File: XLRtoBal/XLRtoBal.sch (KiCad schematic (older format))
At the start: 53 parts, among them J1 XLR3, J10 Conn_Coaxial, J11 Conn_Coaxial, J2 Conn_01x04, J3 Conn_01x04, J4 XLR3, J5 Conn_01x04, J6 Conn_01x01, J7 Conn_01x01, J8 Conn_01x01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

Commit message: Fixed XLR footprint
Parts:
- J1, J4: footprint XLRtoBal:XLR04WP -> XLRtoBal:IOXLR3FEH
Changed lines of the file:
@@
 F 0 "J1" H 2500 2100 50  0000 C CNN
 F 1 "XLR3" H 2550 1600 50  0000 C CNN
-F 2 "XLRtoBal:XLR04WP" H 2350 1850 50  0001 C CNN
+F 2 "XLRtoBal:IOXLR3FEH" H 2350 1850 50  0001 C CNN
 F 3 "" H 2350 1850 50  0001 C CNN
 	1    2350 1850
@@
 F 0 "J4" H 2500 4800 50  0000 C CNN
 F 1 "XLR3" H 2550 4300 50  0000 C CNN
-F 2 "XLRtoBal:XLR04WP" H 2350 4550 50  0001 C CNN
+F 2 "XLRtoBal:IOXLR3FEH" H 2350 4550 50  0001 C CNN
 F 3 "" H 2350 4550 50  0001 C CNN
 	1    2350 4550

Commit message: Changed bootstrap capacitor
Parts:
- removed C17, C5: CB, Capacitors_THT:C_Disc_D5.0mm_W2.5mm_P5.00mm, symbol C_Small
- added C17, C5: 220 uF, Capacitors_THT:CP_Radial_D8.0mm_P5.00mm, symbol CP_Small
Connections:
- net at JP1.2, U1.5 (CM): now also C5.2
- net at J2.2 (Pin_2), U1.8 (CMOUT): now also C5.1
- net at JP2.2, U2.5 (CM): now also C17.2
- net at J5.2 (Pin_2), U2.8 (CMOUT): now also C17.1
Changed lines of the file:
@@
-$EndComp
-$Comp
-L C_Small C5
-U 1 1 5F3D4D81
-P 5350 2850
-F 0 "C5" V 5450 2800 50  0000 L CNN
-F 1 "CB" V 5200 2800 50  0000 L CNN
-F 2 "Capacitors_THT:C_Disc_D5.0mm_W2.5mm_P5.00mm" H 5350 2850 50  0001 C CNN
-F 3 "" H 5350 2850 50  0001 C CNN
-	1    5350 2850
-	0    -1   -1   0
 $EndComp
 $Comp
@@
 	1    0    0    -1
 $EndComp
-$Comp
-L C_Small C17
-U 1 1 5F3DABDA
-P 5350 5550
-F 0 "C17" V 5450 5500 50  0000 L CNN
-F 1 "CB" V 5200 5500 50  0000 L CNN
-F 2 "Capacitors_THT:C_Disc_D5.0mm_W2.5mm_P5.00mm" H 5350 5550 50  0001 C CNN
-F 3 "" H 5350 5550 50  0001 C CNN
-	1    5350 5550
-	0    -1   -1   0
-$EndComp
 Wire Wire Line
 	1800 5300 1800 4550
@@
 	5800 1600 6400 1600
 Connection ~ 5800 2150
+$Comp
+L CP_Small C17
+U 1 1 5F3DF8BC
+P 5350 5550
+F 0 "C17" H 5360 5620 50  0000 L CNN
+F 1 "220 uF" H 5360 5470 50  0000 L CNN
+F 2 "Capacitors_THT:CP_Radial_D8.0mm_P5.00mm" H 5350 5550 50  0001 C CNN
+F 3 "" H 5350 5550 50  0001 C CNN
+	1    5350 5550
+	0    1    1    0
+$EndComp
+$Comp
+L CP_Small C5
+U 1 1 5F3DFCF8
+P 5350 2850
+F 0 "C5" H 5360 2920 50  0000 L CNN
+F 1 "220 uF" H 5360 2770 50  0000 L CNN
+F 2 "Capacitors_THT:CP_Radial_D8.0mm_P5.00mm" H 5350 2850 50  0001 C CNN
+F 3 "" H 5350 2850 50  0001 C CNN
+	1    5350 2850
+	0    1    1    0
+$EndComp
 $EndSCHEMATC

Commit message: Added soft start circuit
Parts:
- added C19, C20: 100 nF, Capacitors_THT:C_Disc_D5.0mm_W2.5mm_P5.00mm, symbol C_Small
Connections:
- net GND: now also C19.2, C20.2
- net at J6.1 (Pin_1): now also C19.1
- net at J8.1 (Pin_1): now also C20.1
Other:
- moved on the sheet: J8, J9
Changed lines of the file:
@@
 L Conn_01x01 J8
 U 1 1 5F3DBD39
-P 9050 5050
-F 0 "J8" H 9050 5150 50  0000 C CNN
-F 1 "Conn_01x01" H 9050 4950 50  0000 C CNN
-F 2 "Connectors:1pin" H 9050 5050 50  0001 C CNN
-F 3 "" H 9050 5050 50  0001 C CNN
-	1    9050 5050
+P 9250 5050
+F 0 "J8" H 9250 5150 50  0000 C CNN
+F 1 "Conn_01x01" H 9250 4950 50  0000 C CNN
+F 2 "Connectors:1pin" H 9250 5050 50  0001 C CNN
+F 3 "" H 9250 5050 50  0001 C CNN
+	1    9250 5050
 	1    0    0    -1
 $EndComp
@@
 L Conn_01x01 J9
 U 1 1 5F3DBDE4
-P 9050 5550
-F 0 "J9" H 9050 5650 50  0000 C CNN
-F 1 "Conn_01x01" H 9050 5450 50  0000 C CNN
-F 2 "Connectors:1pin" H 9050 5550 50  0001 C CNN
-F 3 "" H 9050 5550 50  0001 C CNN
-	1    9050 5550
+P 9250 5550
+F 0 "J9" H 9250 5650 50  0000 C CNN
+F 1 "Conn_01x01" H 9250 5450 50  0000 C CNN
+F 2 "Connectors:1pin" H 9250 5550 50  0001 C CNN
+F 3 "" H 9250 5550 50  0001 C CNN
+	1    9250 5550
 	1    0    0    -1
 $EndComp
@@
 	0    1    1    0
 $EndComp
+$Comp
+L C_Small C19
+U 1 1 5F40299A
+P 7900 5050
+F 0 "C19" V 8050 5000 50  0000 L CNN
+F 1 "100 nF" V 7800 4900 50  0000 L CNN
+F 2 "Capacitors_THT:C_Disc_D5.0mm_W2.5mm_P5.00mm" H 7900 5050 50  0001 C CNN
+F 3 "" H 7900 5050 50  0001 C CNN
+	1    7900 5050
+	0    1    1    0
+$EndComp
+Wire Wire Line
+	8100 5050 8000 5050
+$Comp
+L C_Small C20
+U 1 1 5F403030
+P 8850 5050
+F 0 "C20" V 9000 5000 50  0000 L CNN
+F 1 "100 nF" V 8750 4900 50  0000 L CNN
+F 2 "Capacitors_THT:C_Disc_D5.0mm_W2.5mm_P5.00mm" H 8850 5050 50  0001 C CNN
+F 3 "" H 8850 5050 50  0001 C CNN
+	1    8850 5050
+	0    1    1    0
+$EndComp
+Wire Wire Line
+	9050 5050 8950 5050
+$Comp
+L GND #PWR033
+U 1 1 5F4033A3
+P 7650 5200
+F 0 "#PWR033" H 7650 4950 50  0001 C CNN
+F 1 "GND" H 7650 5050 50  0000 C CNN
+F 2 "" H 7650 5200 50  0001 C CNN
+F 3 "" H 7650 5200 50  0001 C CNN
+	1    7650 5200
+	1    0    0    -1
+$EndComp
+Wire Wire Line
+	7650 5200 7650 5050
+Wire Wire Line
+	7650 5050 7800 5050
+$Comp
+L GND #PWR034
+U 1 1 5F403644
+P 8600 5250
+F 0 "#PWR034" H 8600 5000 50  0001 C CNN
+F 1 "GND" H 8600 5100 50  0000 C CNN
+F 2 "" H 8600 5250 50  0001 C CNN
+F 3 "" H 8600 5250 50  0001 C CNN
+	1    8600 5250
+	1    0    0    -1
+$EndComp
+Wire Wire Line
+	8600 5250 8600 5050
+Wire Wire Line
+	8600 5050 8750 5050
 $EndSCHEMATC

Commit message: Submitted to JLCPCB 2020-08-24
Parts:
- C1, C13, C14, C2: LCSC (none) -> C263196
- C10, C11, C12, C16, C18, C19, C20, C4, C6, C7: LCSC (none) -> C454377
- C15, C3: LCSC (none) -> C400081
- C17, C5: LCSC (none) -> C239308
- C8, C9: LCSC (none) -> C125770
- D1, D10, D2, D3, D4, D7, D8, D9: LCSC (none) -> C14516
- D5, D6: LCSC (none) -> C36751
- J1, J4: value XLR3 -> XLR-04WP; LCSC (none) -> C558741
- J10, J11: value Conn_Coaxial -> SMAPCB; LCSC (none) -> C496549
- J2, J3, J5: LCSC (none) -> C395849
- Q1: LCSC (none) -> C358526
- Q2: LCSC (none) -> C358527
- R1, R2, R7, R8: LCSC (none) -> C57438
- R3, R4: value 4k7 -> 6k8; LCSC (none) -> C176446
- R5, R6: value 1k -> 2k2; LCSC (none) -> C58595
- U1, U2: LCSC (none) -> C115171

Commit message: Changed to 2N5551/2N5401 from BC546C/BC556C transistors
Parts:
- added D11, D12: LED, LEDs:LED_D3.0mm, symbol LED
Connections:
- net GND: now also D12.1 (K); no longer R6.1
- net VEE: now also D11.1 (K); no longer R5.1
- new net: D12.2 (A), R6.1
- new net: D11.2 (A), R5.1
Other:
- moved on the sheet: R5, R6

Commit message: Some more layout changed and XlrtoBal fix
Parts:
- added R10, R9: 4k7, Resistors_THT:R_Axial_DIN0207_L6.3mm_D2.5mm_P7.62mm_Horizontal, symbol R
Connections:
- net at C1.1, C2.2, C3.2: now also R9.1
- net at C5.1, J2.2 (Pin_2), U1.8 (CMOUT): now also R9.2
- net at C13.1, C14.2, C15.2: now also R10.1
- net at C17.1, J5.2 (Pin_2), U2.8 (CMOUT): now also R10.2
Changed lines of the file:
@@
 	3300 2600 3850 2600
 Wire Wire Line
-	3650 2700 3650 2250
+	3650 1650 3650 2700
 Wire Wire Line
 	3650 2250 3400 2250
@@
 	3300 5300 3850 5300
 Wire Wire Line
-	3650 5400 3650 4950
+	3650 4350 3650 5400
 Wire Wire Line
 	3650 4950 3400 4950
@@
 Wire Wire Line
 	10500 2550 10500 2450
+$Comp
+L R R10
+U 1 1 5F62CB3D
+P 3650 4200
+F 0 "R10" V 3730 4200 50  0000 C CNN
+F 1 "4k7" V 3650 4200 50  0000 C CNN
+F 2 "Resistors_THT:R_Axial_DIN0207_L6.3mm_D2.5mm_P7.62mm_Horizontal" V 3580 4200 50  0001 C CNN
+F 3 "" H 3650 4200 50  0001 C CNN
+F 4 "C57438" V 3650 4200 60  0001 C CNN "LCSC"
+	1    3650 4200
+	-1   0    0    1
+$EndComp
+Connection ~ 3650 4950
+Wire Wire Line
+	3650 4050 3650 3850
+Wire Wire Line
+	3650 3850 5600 3850
+Wire Wire Line
+	5600 3850 5600 4650
+Connection ~ 5600 4650
+$Comp
+L R R9
+U 1 1 5F62D237
+P 3650 1500
+F 0 "R9" V 3730 1500 50  0000 C CNN
+F 1 "4k7" V 3650 1500 50  0000 C CNN
+F 2 "Resistors_THT:R_Axial_DIN0207_L6.3mm_D2.5mm_P7.62mm_Horizontal" V 3580 1500 50  0001 C CNN
+F 3 "" H 3650 1500 50  0001 C CNN
+F 4 "C57438" V 3650 1500 60  0001 C CNN "LCSC"
+	1    3650 1500
+	-1   0    0    1
+$EndComp
+Connection ~ 3650 2250
+Wire Wire Line
+	3650 1350 3650 1100
+Wire Wire Line
+	3650 1100 5600 1100
+Wire Wire Line
+	5600 1100 5600 1950
+Connection ~ 5600 1950
 $EndSCHEMATC

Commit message: Changed grounding and star layout
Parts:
- removed C19, C20: 100 nF, Capacitors_THT:C_Disc_D5.0mm_W2.5mm_P5.00mm, symbol C_Small
- removed J1, J4: XLR-04WP, XLRtoBal:IOXLR3FEH, symbol XLR3
- added J1, J4: XLR4BODYPIN, symbol XLR4BODYPIN
- added J12: Conn_01x02, Connectors_Terminal_Blocks:TerminalBlock_bornier-2_P5.08mm, symbol Conn_01x02
- added JP3, JP4: Jumper_NO_Small, Pin_Headers:Pin_Header_Straight_1x02_Pitch2.54mm, symbol Jumper_NO_Small
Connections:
- net GND: now also J1.1, J1.G, J12.1 (Pin_1), J12.2 (Pin_2), J4.1, J4.G, JP3.1, JP4.1
- net at D3.2 (A), D4.1 (K), R1.2: now also J1.2
- net at D1.2 (A), D2.1 (K), R2.2: now also J1.3
- net at D7.2 (A), D8.1 (K), R7.2: now also J4.2
- net at D10.1 (K), D9.2 (A), R8.2: now also J4.3
- net at J6.1 (Pin_1): now also JP3.2
- net at J8.1 (Pin_1): now also JP4.2
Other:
- moved on the sheet: J6, J7, J8, J9

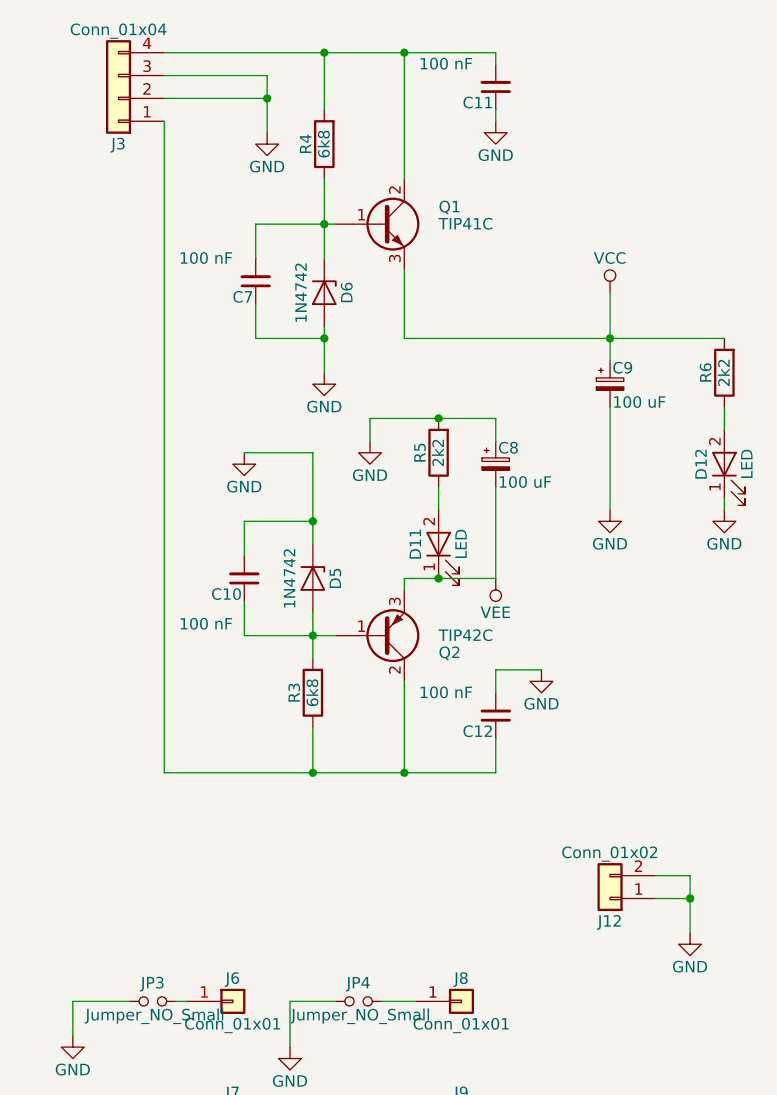
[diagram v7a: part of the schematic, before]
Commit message: Added option for spade terminal power connections
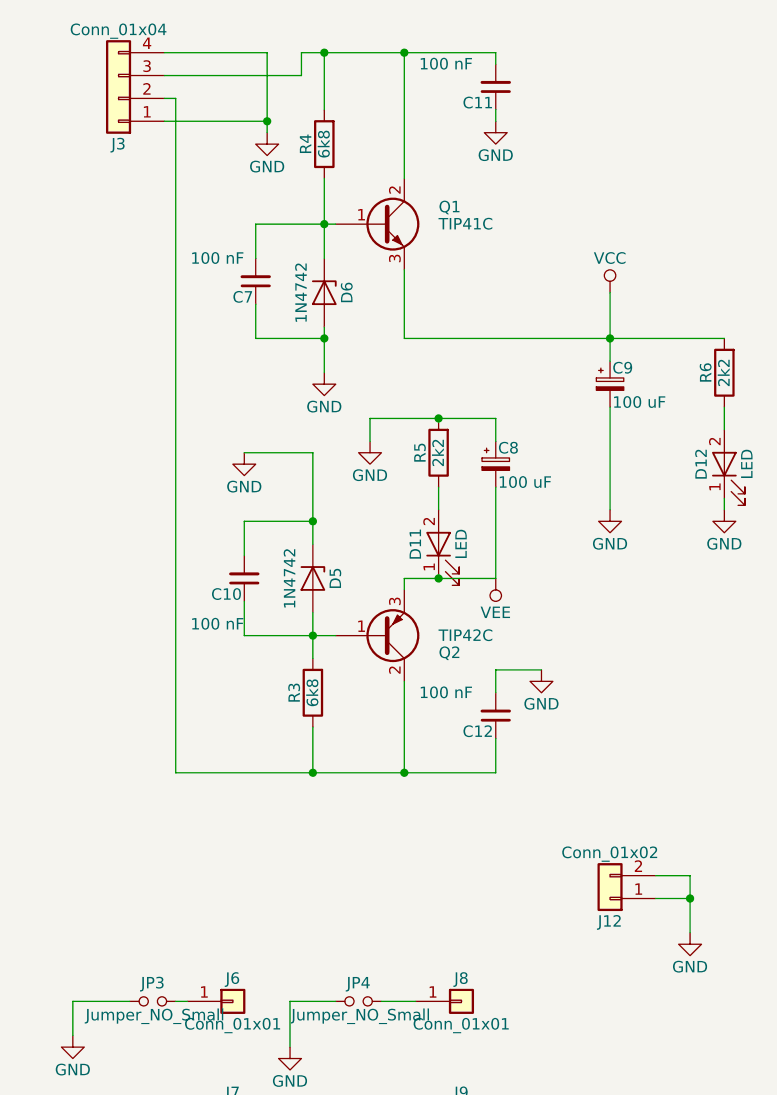
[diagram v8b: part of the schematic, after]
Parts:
- J12: footprint Connectors_Terminal_Blocks:TerminalBlock_bornier-2_P5.08mm -> XLRtoBal:TerminalBlock_bornier-2_P5.08mm_with_spade
- J3: footprint Connectors_Terminal_Blocks:TerminalBlock_bornier-4_P5.08mm -> XLRtoBal:TerminalBlock_bornier-4_P5.08mm_with_spade
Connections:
- net GND: now also J3.1 (Pin_1), J3.4 (Pin_4); no longer J3.2 (Pin_2), J3.3 (Pin_3)
- net at C12.1, Q2.2 (C), R3.1: now also J3.2 (Pin_2); no longer J3.1 (Pin_1)
- net at C11.2, Q1.2 (C), R4.2: now also J3.3 (Pin_3); no longer J3.4 (Pin_4)
